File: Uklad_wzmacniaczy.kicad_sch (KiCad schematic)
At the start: 79 parts, among them J1 MEM2080-00-128-00-A, U1 OPA2388IDR, U10 LD1117S50TR_SOT223, U11 LT3094EMSE-TRPBF, U2 REF2033QDDCRQ1, U3 AD8421ARMZ, U4 OPA388IDR, U5 AD8421ARMZ, U6 TPD4E1B06DRLR, U7 LT3042EMSE-TRPBF, U8 TPS65135RTER, U9 TPS61236PRWLR

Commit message: Footprint and symbol for Nucleo-h755ZIQ added
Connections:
- net +1.65V is gone; now on net +1.65VA: R2.1, R6.2, R8.2, R9.2
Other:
- added sheet Nucleo (untitled.kicad_sch)
- moved on the sheet: C22, R8, R9

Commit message: PCB layout first commit, minor fix in schematic
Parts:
- added J2: SJ1-3523N, Uklad_wzmacniaczy_footprints:CUI_SJ1-3523N, symbol Amplifier_circuit:SJ1-3523N
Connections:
- net +3.3V: now also C22.1, J1.P4 (VDD)
- net Analog_In1: now also J2.3
- net Analog_In2: now also J2.2
- net Reference_In: now also J2.1
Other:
- sheet Nucleo: file untitled.kicad_sch -> Nucleo.kicad_sch
- sheet Nucleo ports: added DETECT_SD, SDMMC_CK, SDMMC_CMD, SDMMC_D0, SDMMC_D1, SDMMC_D2, SDMMC_D3, TO_ADC1, TO_ADC2; removed none
- note added: "Nucleo Footprint"
- moved on the sheet: C1, C10, C11, C12, C13, C14, C15, C16, C17, C18, C19, C2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

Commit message: Schematic minor change Vbat -> 3.3V, PCB layout: +5V, -5V
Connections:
- net +3.3V: now also U8.8 (EN)
- net +BATT: no longer U8.8 (EN)
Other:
- note added: "Dodać potencjometry cyfrowe oraz gniazda do podpięcia czujników rezystancyjnych"
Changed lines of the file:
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@@
 		)
 	)
+	(text "Dodać potencjometry cyfrowe oraz gniazda do podpięcia czujników rezystancyjnych"
+		(exclude_from_sim no)
+		(at 272.034 -18.288 0)
+		(effects
+			(font
+				(size 10 10)
+			)
+		)
+	)
 	(text "Nucleo\nFootprint"
 		(exclude_from_sim no)
@@
 	)
 	(symbol
-		(lib_id "power:+BATT")
-		(at 73.66 207.01 90)
-		(unit 1)
-		(exclude_from_sim no)
-		(in_bom yes)
-		(on_board yes)
-		(dnp no)
-		(fields_autoplaced yes)
-		(property "Reference" "#PWR046"
-			(at 77.47 207.01 0)
-			(effects
-				(font
-					(size 1.27 1.27)
-				)
-				(hide yes)
-			)
-		)
-		(property "Value" "+BATT"
-			(at 69.85 207.0099 90)
-			(effects
-				(font
-					(size 1.27 1.27)
-				)
-				(justify left)
-			)
-		)
-		(property "Footprint" ""
-			(at 73.66 207.01 0)
-			(effects
-				(font
-					(size 1.27 1.27)
-				)
-				(hide yes)
-			)
-		)
-		(property "Datasheet" ""
-			(at 73.66 207.01 0)
-			(effects
-				(font
-					(size 1.27 1.27)
-				)
-				(hide yes)
-			)
-		)
-		(property "Description" "Power symbol creates a global label with name \"+BATT\""
-			(at 73.66 207.01 0)
-			(effects
-				(font
-					(size 1.27 1.27)
-				)
-				(hide yes)
-			)
-		)
-		(pin "1"
-		)
-		(instances
-			(project "Uklad_wzmacniaczy"
-				(path "/5beef803-c264-4e64-a820-2636d42e5954"
-					(reference "#PWR046")
-					(unit 1)
-				)
-			)
-		)
-	)
-	(symbol
 		(lib_id "power:GND")
 		(at 181.61 199.39 0)
@@
 					(unit 1)
 				)
+			)
+		)
+	)
+	(symbol
+		(lib_id "power:+3.3V")
+		(at 73.66 207.01 90)
+		(unit 1)
+		(exclude_from_sim no)
+		(in_bom yes)
+		(on_board yes)
+		(dnp no)
+		(property "Reference" "#PWR046"
+			(at 77.47 207.01 0)
+			(effects
+				(font
+					(size 1.27 1.27)
+				)
+				(hide yes)
+			)
+		)
+		(property "Value" "+3.3V"
+			(at 67.818 207.01 90)
+			(effects
+				(font
+					(size 1.27 1.27)
+				)
+			)
+		)
+		(property "Footprint" ""
+			(at 73.66 207.01 0)
+			(effects
+				(font
+					(size 1.27 1.27)
+				)
+				(hide yes)
+			)
+		)
+		(property "Datasheet" ""
+			(at 73.66 207.01 0)
+			(effects
+				(font
+					(size 1.27 1.27)
+				)
+				(hide yes)
+			)
+		)
+		(property "Description" "Power symbol creates a global label with name \"+3.3V\""
+			(at 73.66 207.01 0)
+			(effects
+				(font
+					(size 1.27 1.27)
+				)
+				(hide yes)
+			)
+		)
+		(pin "1"
+		)
+		(instances
+			(project "Uklad_wzmacniaczy"
+				(path "/5beef803-c264-4e64-a820-2636d42e5954"
+					(reference "#PWR046")
+					(unit 1)
+				)

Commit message: New STM footprint, changed PCB layout, added pin connector
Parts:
- removed C27, C38, C39: 10u, Capacitor_SMD:C_0603_1608Metric_Pad1.08x0.95mm_HandSolder, symbol Device:C
- removed C28: 1u, Capacitor_SMD:C_0603_1608Metric_Pad1.08x0.95mm_HandSolder, symbol Device:C
- removed C31: 10p, Capacitor_SMD:C_0603_1608Metric_Pad1.08x0.95mm_HandSolder, symbol Device:C
- removed C32, C33, C34: 22u, Capacitor_SMD:C_0603_1608Metric_Pad1.08x0.95mm_HandSolder, symbol Device:C
- removed C36: 10n, Capacitor_SMD:C_0603_1608Metric_Pad1.08x0.95mm_HandSolder, symbol Device:C
- removed D1: LED, LED_SMD:LED_0805_2012Metric_Pad1.15x1.40mm_HandSolder, symbol Device:LED
- removed L1: 1u, Uklad_wzmacniaczy_footprints:IND_SPM6530T-1R0M120, symbol Device:L
- removed R12: 1M, Resistor_SMD:R_0603_1608Metric_Pad0.98x0.95mm_HandSolder, symbol Device:R
- removed R14: 332k, Resistor_SMD:R_0603_1608Metric_Pad0.98x0.95mm_HandSolder, symbol Device:R
- removed R15: 2k, Resistor_SMD:R_0603_1608Metric_Pad0.98x0.95mm_HandSolder, symbol Device:R
- removed R16: 41.2k, Resistor_SMD:R_0603_1608Metric_Pad0.98x0.95mm_HandSolder, symbol Device:R
- removed U10: LD1117S50TR_SOT223, Package_TO_SOT_SMD:SOT-223-3_TabPin2, symbol Regulator_Linear:LD1117S50TR_SOT223
- removed U9: TPS61236PRWLR, Uklad_wzmacniaczy_footprints:RWL0009A, symbol Amplifier_circuit:TPS61236PRWLR
- added J3: Conn_01x10_Pin, Connector_PinHeader_2.54mm:PinHeader_2x05_P2.54mm_Horizontal, symbol Connector:Conn_01x10_Pin
- added U10, U11, U7: AD5162BRMZ10-RL7, Uklad_wzmacniaczy_footprints:RM_10_ADI, symbol Amplifier_circuit:AD5162BRMZ10-RL7
- renumbered C29 to C27, C30 to C28, C35 to C29, C37 to C30, C40 to C31, C41 to C32, C42 to C33, C43 to C34, J2 to J1, J1 to J2, L2 to L1, R13 to R12, R17 to R13, R18 to R14, R19 to R15, R20 to R16, U11 to U12, U7 to U8, U8 to U9
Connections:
- net +3.3V: now also J3.1 (Pin_1), U10.5 (VDD), U11.5 (VDD), U7.5 (VDD)
- net GND: no longer C1.2, C10.2, C11.2, C12.1, C13.2, C16.2, C17.1, C18.2, C2.2, C20.1, C21.2, C23.2, C24.1, C25.2, C26.2, C27.2, C28.1, C29.2, C3.2, C30.2, C31.2, C32.1, C33.2, C34.2, C4.1, C5.1, C6.2, C7.2, C9.2, R12.1, R15.1, U1.4 (V-), U12.6 (ILIM), U12.9 (GND), U2.2 (GND), U3.6 (REF), U4.4 (V-), U5.6 (REF), U6.2 (GND), U8.5 (ILIM), U8.8 (GND), U9.11 (PGND), U9.12 (PGND), U9.5 (GND)
- new net CLK: U10.6 (CLK), U11.6 (CLK), U7.6 (CLK)
- new net CS_1: U7.8 (CS*)
- new net CS_2: U10.8 (CS*)
- new net CS_3: U11.8 (CS*)
- new net GNDA: C1.2, C10.2, C11.2, C12.1, C13.2, C16.2, C17.1, C18.2, C2.2, C20.1, C21.2, C23.2, C24.1, C25.2, C26.2, C27.2, C28.1, C29.2, C3.2, C30.2, C31.2, C32.1, C33.2, C34.2, C4.1, C5.1, C6.2, C7.2, C9.2, J3.8 (Pin_8), R12.1, R15.1, U1.4 (V-), U10.1 (B1), U10.4 (GND), U10.9 (B2), U11.1 (B1), U11.4 (GND), U11.9 (B2), U12.6 (ILIM), U12.9 (GND), U2.2 (GND), U3.6 (REF), U4.4 (V-), U5.6 (REF), U6.2 (GND), U7.1 (B1), U7.4 (GND), U7.9 (B2), U8.5 (ILIM), U8.8 (GND), U9.11 (PGND), U9.12 (PGND), U9.5 (GND)
- new net SDI: U10.7 (SDI), U11.7 (SDI), U7.7 (SDI)
- new net SIG_1: J3.2 (Pin_2), U7.10 (W1)
- new net SIG_2: J3.3 (Pin_3), U7.3 (W2)
- new net SIG_3: J3.4 (Pin_4), U10.10 (W1)
- new net SIG_4: J3.5 (Pin_5), U10.3 (W2)
- new net SIG_5: J3.6 (Pin_6), U11.10 (W1)
- new net SIG_6: J3.7 (Pin_7), U11.3 (W2)
- no-connect marks 7 -> 11
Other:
- sheet Nucleo ports: added +3.3V, +BATT, SIG_1, SIG_2, SIG_3, SIG_4, SIG_5; removed none
- note added: "Nucleo Pinout"
- note added: "PLAN: [x] DODAĆ SLOT MICRO SD [x] WZMACNIACZ INSTRUMENTAL [x] WZMACNIACZ 2 STOPNIA [x] NAPIĘCIE ODNIESIENIA 1,65v [x] NAPIĘCIE ODNIESIENIA +5V I -5V [x] ZASILANIE 5V [x] DODAĆ DIGIPOT"
- note added: "Potencjometry cyfrowe"
- note removed: "Dodać potencjometry cyfrowe oraz gniazda do podpięcia czujników rezystancyjnych"
- note removed: "Nucleo Footprint"
- note removed: "PLAN: [x] DODAĆ SLOT MICRO SD [x] WZMACNIACZ INSTRUMENTAL [x] WZMACNIACZ 2 STOPNIA [x] NAPIĘCIE ODNIESIENIA 1,65v [x] NAPIĘCIE ODNIESIENIA +5V I -5V [x] ZASILANIE 5V"
- note removed: "Źródło zasilania +5V i +3.3V"

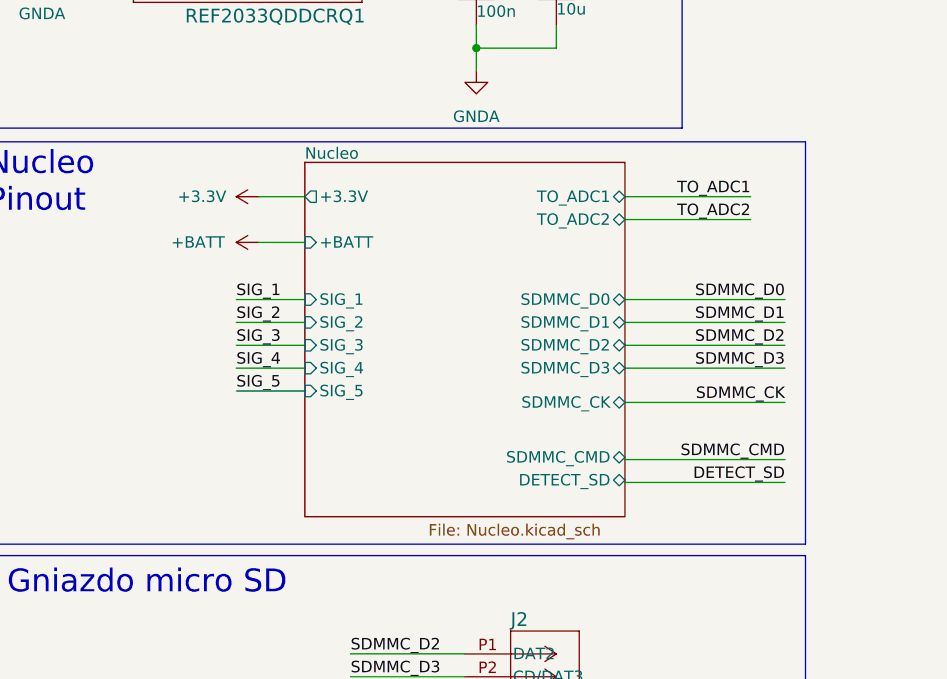
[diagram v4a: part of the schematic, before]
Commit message: Nucleo-shield pins change
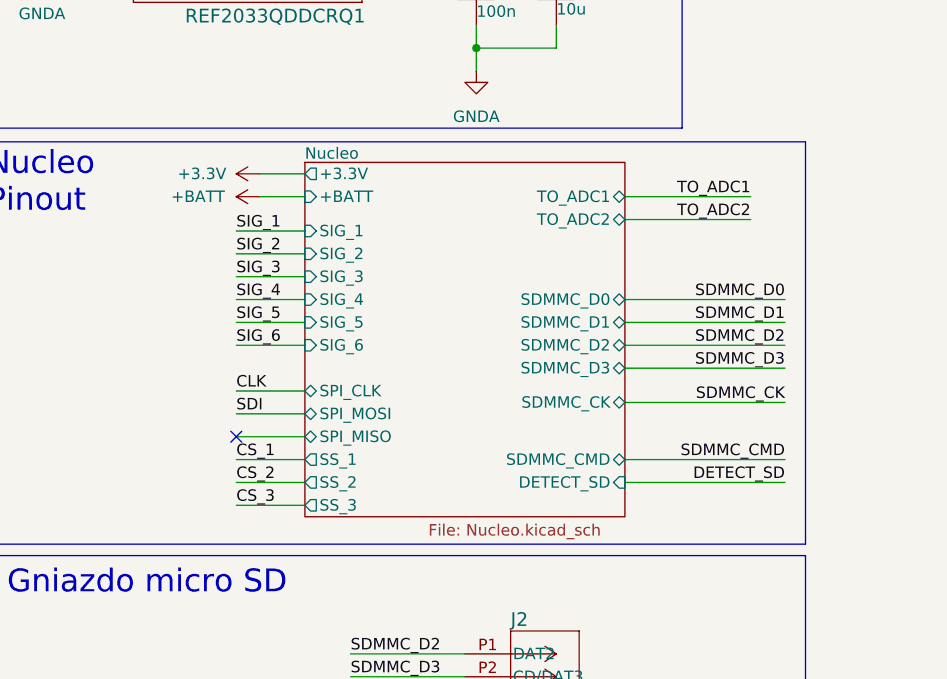
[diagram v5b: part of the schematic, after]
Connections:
- no-connect marks 11 -> 12
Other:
- sheet Nucleo ports: added SIG_6, SPI_CLK, SPI_MISO, SPI_MOSI, SS_1, SS_2, SS_3; removed none

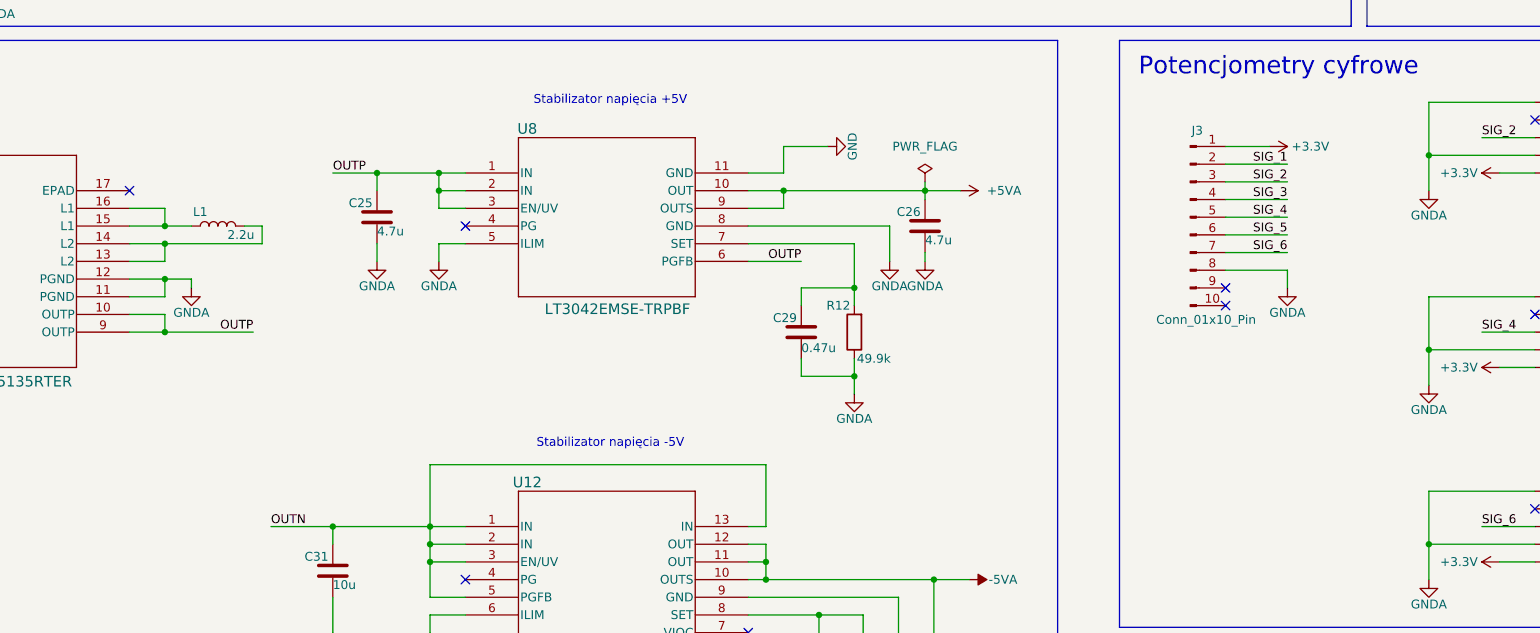
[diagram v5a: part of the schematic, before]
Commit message: Layout major change, .gitignore added
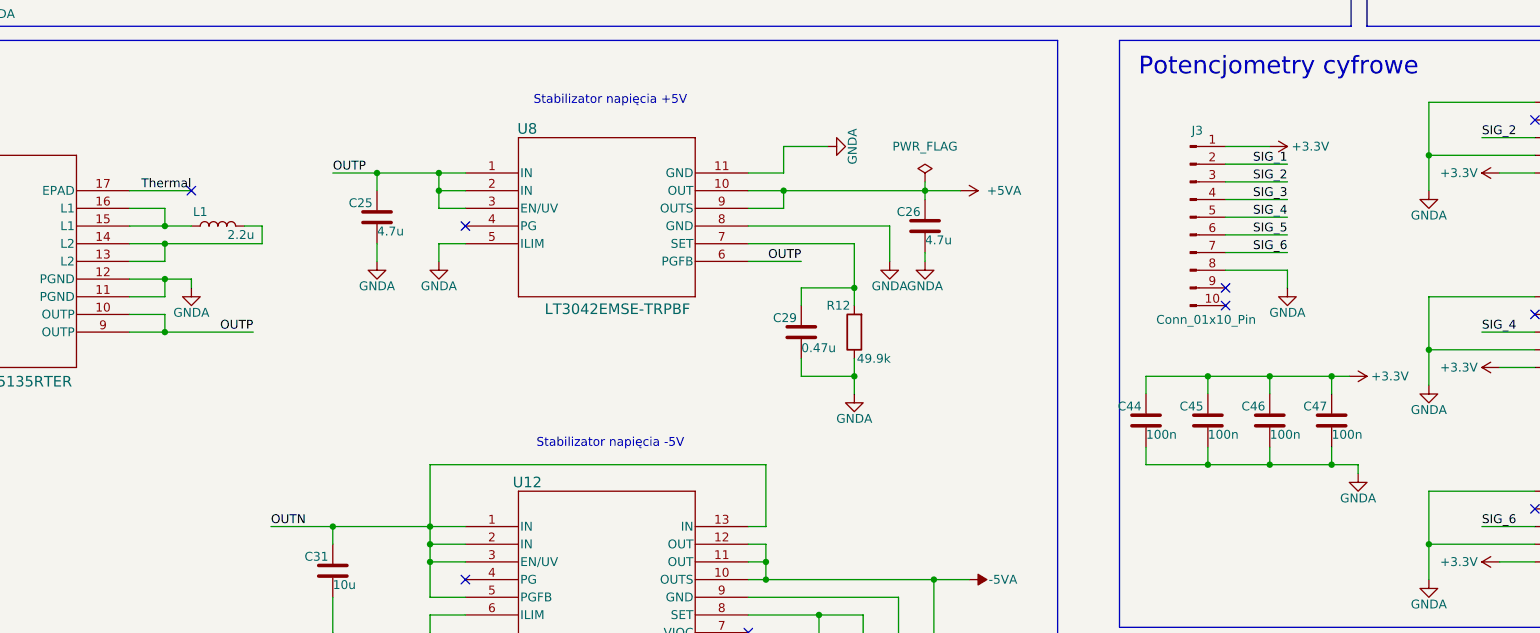
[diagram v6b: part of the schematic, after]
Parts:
- added C44, C45, C46, C47: 100n, Capacitor_SMD:C_0603_1608Metric_Pad1.08x0.95mm_HandSolder, symbol Device:C
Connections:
- net +3.3V: now also C44.1, C45.1, C46.1, C47.1
- net GND: no longer U8.11 (GND)
- net GNDA: now also U8.11 (GND), C44.2, C45.2, C46.2, C47.2
- net Thermal: now reaches U9.17 (EPAD)

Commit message: Layout and schematic minor changes
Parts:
- added TP1: 3,3V, TestPoint:TestPoint_Pad_D1.5mm, symbol Connector:TestPoint
- added TP10: POT2, TestPoint:TestPoint_Pad_D1.5mm, symbol Connector:TestPoint
- added TP11: POT3, TestPoint:TestPoint_Pad_D1.5mm, symbol Connector:TestPoint
- added TP12: POT4, TestPoint:TestPoint_Pad_D1.5mm, symbol Connector:TestPoint
- added TP13: POT5, TestPoint:TestPoint_Pad_D1.5mm, symbol Connector:TestPoint
- added TP14: POT6, TestPoint:TestPoint_Pad_D1.5mm, symbol Connector:TestPoint
- added TP15: GND, TestPoint:TestPoint_Pad_2.0x2.0mm, symbol Connector:TestPoint
- added TP16: +BATT, TestPoint:TestPoint_Pad_D1.5mm, symbol Connector:TestPoint
- added TP17, TP5: GNDA, TestPoint:TestPoint_Pad_2.0x2.0mm, symbol Connector:TestPoint
- added TP2: 5V, TestPoint:TestPoint_Pad_D1.5mm, symbol Connector:TestPoint
- added TP3: +5V, TestPoint:TestPoint_Pad_D1.5mm, symbol Connector:TestPoint
- added TP4: -5V, TestPoint:TestPoint_Pad_D1.5mm, symbol Connector:TestPoint
- added TP6: 1,65V, TestPoint:TestPoint_Pad_D1.5mm, symbol Connector:TestPoint
- added TP7: ADC1, TestPoint:TestPoint_Pad_D1.5mm, symbol Connector:TestPoint
- added TP8: ADC2, TestPoint:TestPoint_Pad_D1.5mm, symbol Connector:TestPoint
- added TP9: POT1, TestPoint:TestPoint_Pad_D1.5mm, symbol Connector:TestPoint
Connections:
- net Thermal is gone; now on net GNDA: U9.17 (EPAD)
- net +1.65VA: now also TP6.1
- net +3.3V: now also TP1.1
- net +5VA: now also TP3.1
- net +BATT: now also TP16.1
- net -5VA: now also TP4.1
- net GND: now also TP15.1
- net GNDA: now also TP17.1, TP5.1
- net SIG_1: now also TP9.1
- net SIG_2: now also TP10.1
- net SIG_3: now also TP11.1
- net SIG_4: now also TP12.1
- net SIG_5: now also TP13.1
- net SIG_6: now also TP14.1
- net TO_ADC1: now also TP7.1
- net TO_ADC2: now also TP8.1
- new net +5V: TP2.1
- no-connect marks 12 -> 11
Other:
- note added: "Test points"
